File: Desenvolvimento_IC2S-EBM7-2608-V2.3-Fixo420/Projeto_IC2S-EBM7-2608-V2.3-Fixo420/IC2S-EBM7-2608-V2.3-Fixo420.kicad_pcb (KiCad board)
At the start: 4 copper layers, 60 x 60 mm, 146 parts, among them P1 M20-7822046, P2 M20-7821446, T1 TP_+24V, T2 TP_GND_ADC_P1, T3 TP_DGND, T4 TP_+5V_REG, T5 TP_+3.3V_DIG, T6 TP_+3.3V_ANA, T7 TP_GND_ADC, T8 TP_+24V_ADC, U1 R-78HB5.0-0.5L, U10 TPS26613DDFR, U11 TPS26613DDFR, U12 TPS7A4001DGN, U13 LP5907MFX-2.5, U2 SPX3819M5-L-3-3/TR, U3 SPX3819M5-L-3-3/TR, U4 TL431B, U5 ISO7141CCDBQR, U6 AD7124-8BCPZ, U7 ADR4525BRZ, U8 TPS26613DDFR, U9 TPS26613DDFR

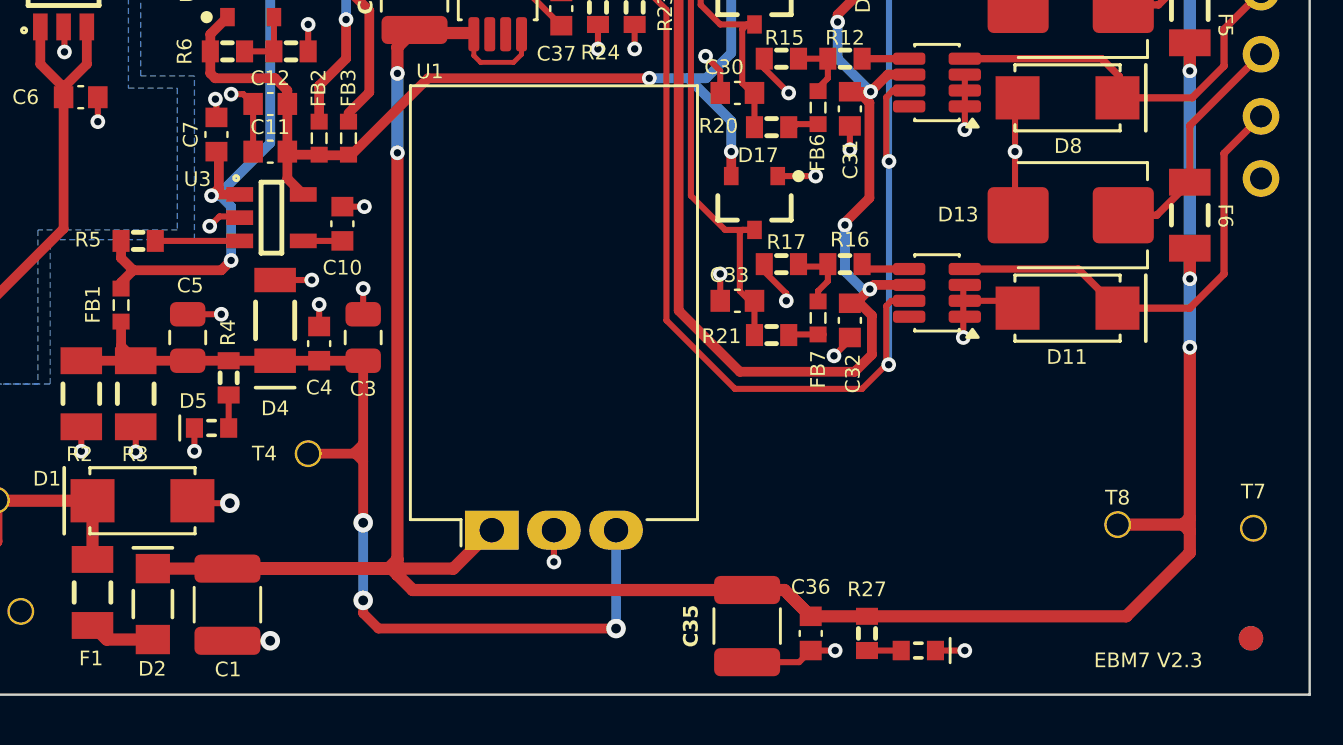
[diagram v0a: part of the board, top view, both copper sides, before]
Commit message: Condensadores do U1 junto dos pinos; pacote de fabricacao regenerado
PCB (28-09 18:19):
- C1 (10 uF/100 V, entrada do R-78HB) a 2,94 mm do pino 1 (era 10,9 mm).
- C3 (22 uF, saida) a 2,32 mm do pino 3 (era 12,4 mm). Recom R-78HB-0.5:
  "C1 and C2 are required and should be fitted close to the converter pins".
- C35/C36/R27 (folha 06) afastados do bordo: C35 de 0,53 para 2,23 mm.
- DRC com paridade: 0 erros, 0 desligados, paridade 0; 1 aviso cosmetico
  (texto C35 sobre o pad do C36).

Doc: corrigida a atribuicao errada do C35 ao U1 e o "C1/C2 do U1" (nomes do
datasheet, nao referencias da placa).

Fabricacao: Gerbers, furacao, PnP, stencil, BOM, vistas, STEP e PDF do
esquematico regenerados desta placa (18:23).

Co-Authored-By: Claude Opus 5.5 (1M context) <noreply@anthropic.com>
Claude-Session: https://claude.ai/code/session_01KPnkiJQKrkjgRqqw9M78ie
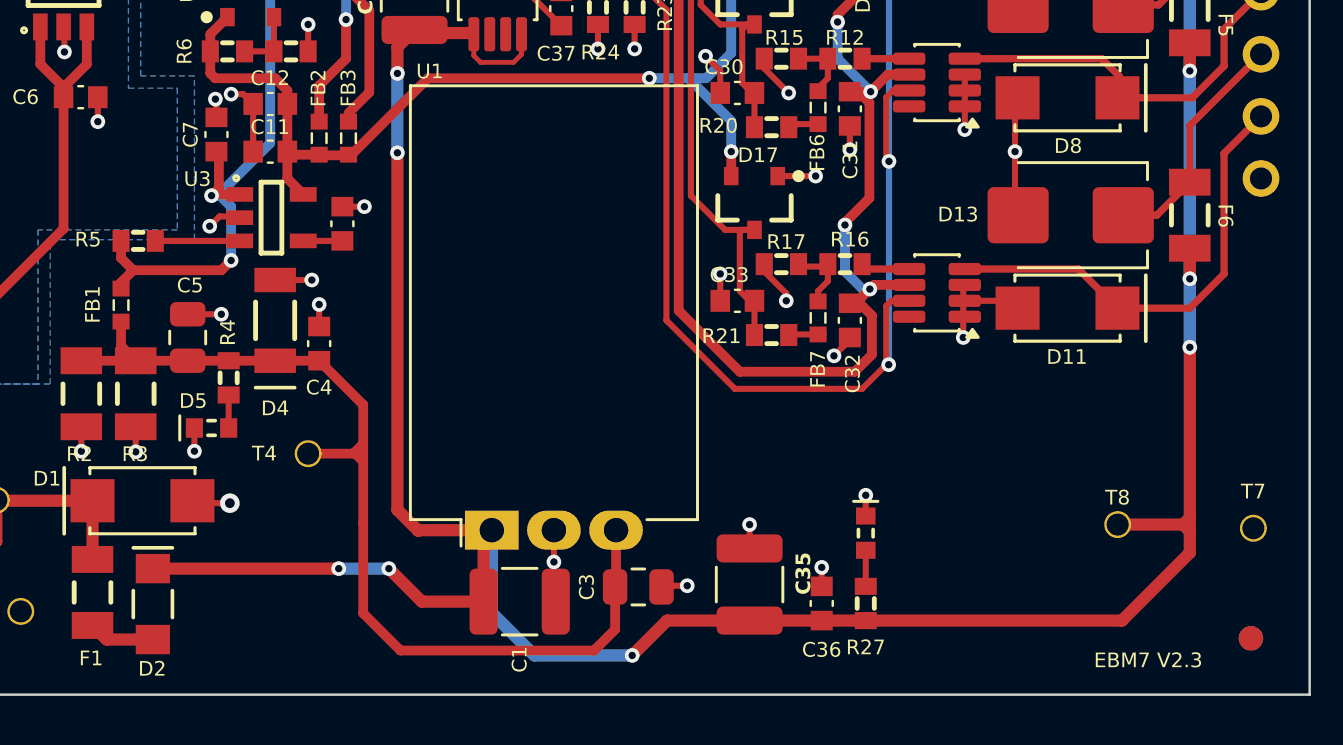
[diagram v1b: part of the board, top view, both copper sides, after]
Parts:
- moved C3 15.2 mm to (151.1, 130.6), turned to 180 degrees
- moved C1 12.0 mm to (146.2, 131.2), turned to 0 degrees
- moved D18 5.26 mm to (160.3, 128.4), turned to -90 degrees
- moved C35 1.70 mm to (155.6, 130.5), turned to 90 degrees
- moved C36 1.31 mm to (158.6, 131.3), turned to 90 degrees
- moved R27 1.23 mm to (160.3, 131.3), turned to 90 degrees
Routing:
- net +24V_ADC: track 129.0 -> 124.3 mm, vias 7 -> 10
- net GND_ADC: track 141.2 -> 137.2 mm
- net +5V_REG: track 42.0 -> 41.7 mm, vias 3 -> 0

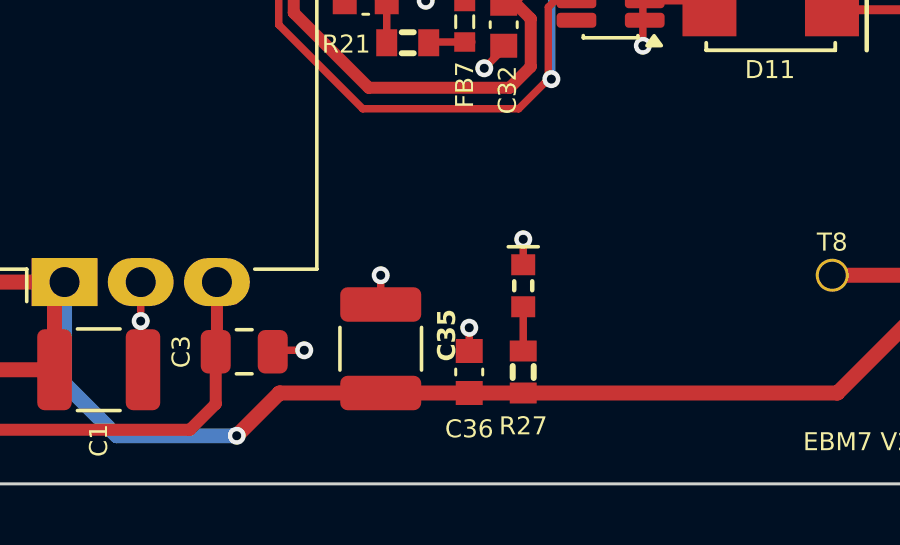
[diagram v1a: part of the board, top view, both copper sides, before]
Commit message: Limpeza do ERC/DRC: fio solto e rotulo duplicado na folha 5, notas do C1 na folha 2, texto do C35
- 05_adc: removido o troco de fio de 1,27 mm em (128,27; 78,74)-(128,27; 80,01)
  com a junction que so existia por ele (extremo sem ligacao no ERC), e o
  rotulo local +2.5_VREF sobreposto ao global em (236,22; 83,82).
- 02_entrada: notas 4 e 12 falavam de "C1/C13" da numeracao antiga; o C13 e
  hoje o bypass do VCC2 do U5. A entrada do U1 (R-78HB) e o C1.
- PCB: texto de serigrafia ${REFERENCE} do C35 afastado do pad do C36.

Netlist do kicad-cli identica pino a pino antes/depois (104 redes;
+2.5_VREF = C24, C25, R8, U6.20, U7.6). DRC com paridade: 0 erros, 0 avisos,
0 desligados, paridade 0. Pacote de fabricacao regenerado.

Co-Authored-By: Claude Opus 5.5 (1M context) <noreply@anthropic.com>
Claude-Session: https://claude.ai/code/session_01KPnkiJQKrkjgRqqw9M78ie
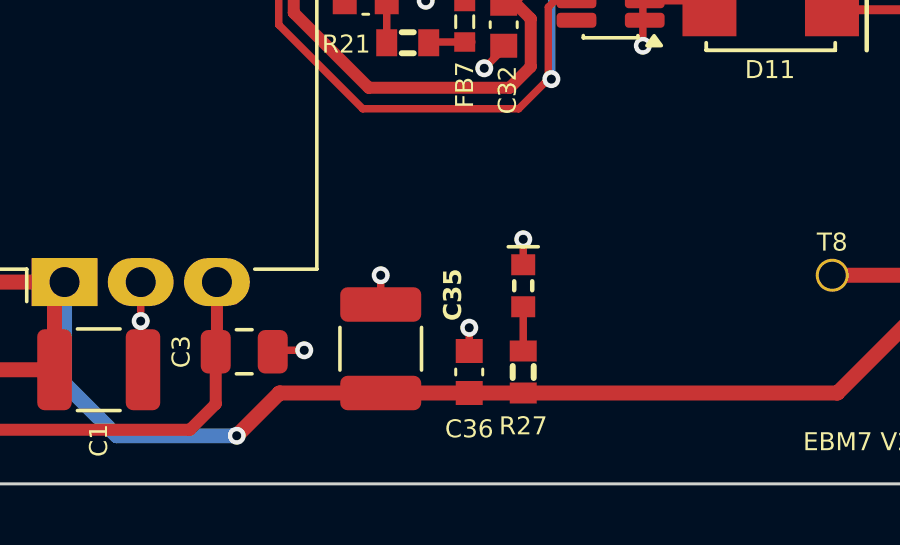
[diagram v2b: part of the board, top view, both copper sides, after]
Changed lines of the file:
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@@
 		)
 		(fp_text user "${REFERENCE}"
-			(at 0.45 2.2 90)
+			(at 1.8 2.4 90)
 			(layer "F.SilkS")
 			(effects

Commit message: PCB: actualizada a partir do esquemático do limitador discreto (sem posicionar)
Equivalente ao F8 (Update PCB from Schematic), feito com ferramentas/atualizar_pcb.py:
- saem U8-U12, R22-R26, C26, C29, C31, C32, C37 e C38 (16);
- entram Q1-Q8, R40-R48, D26 e C50 (19), estacionados abaixo da placa, um canal por linha;
- D6/D7/D8/D11: DO-214 -> DO-214AA (SMBJ36A-13-F), rodados 180 graus. O pad 1 do DO-214AA fica do
  lado oposto ao do DO-214; sem a rotação, a pista AINk caía no pad de GND_ADC;
- R13-R15/R17: 0603R -> 1206R (TNPW1206110RBEEA);
- R10/R11/R12/R16 pad 2 passam a Net-(Q5..Q8-E); as 5 pistas dessas redes seguem o pad;
- U2, C6, C8, C9, T3 e T5 re-ligados ao símbolo pela referência: passaram da folha 3 para a 4 sem
  actualizar a PCB, e o F8 por defeito duplicava-os ou apagava-os. C49 só tinha a folha desactualizada.
Nada mais muda: 882 pistas/vias com a mesma geometria, 11 zonas iguais, sem refill.

DRC: paridade com o esquemático 0 (eram 59). Ficam 104 violações e 44 não ligados, todos do layout
por fazer:
- 8 curtos, 6 clearance e 8 mask bridge: os R13-R17 1206 sobre as pistas AINk_ADC;
- 20 courtyards: 1206 e SMB no sítio antigo;
- 43 pistas soltas do roteamento antigo;
- as peças novas por rotear.
Não fabricar como está.

Co-Authored-By: Claude Opus 5.5 (1M context) <noreply@anthropic.com>
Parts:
- removed C26, C29, C31, C32, C37: 100nF/50V, EBM7_V23:0603C
- removed C38: 10uF/50V, EBM7_V23:C_1206_3216Metric
- removed R22: 11k5, EBM7_V23:0603R
- removed R23, R24: 6k65, EBM7_V23:0603R
- removed R25: 93k1, EBM7_V23:0603R
- removed R26: 10k, EBM7_V23:0603R
- removed U10, U11, U8, U9: TPS26613DDFR, EBM7_V23:SOT-23-8
- removed U12: TPS7A4001DGN, EBM7_V23:HVSSOP-8-1EP
- added C50: 100nF/50V, EBM7_V23:0603C, F.Cu at (124.5, 181.1)
- added D26: BZT52H-C10, EBM7_V23:SOD-123F, F.Cu at (133.5, 181.1)
- added Q1: BSP297, EBM7_V23:SOT-223-3_TabPin2, F.Cu at (124.5, 145.1)
- added Q2: BSP297, EBM7_V23:SOT-223-3_TabPin2, F.Cu at (124.5, 154.1)
- added Q3: BSP297, EBM7_V23:SOT-223-3_TabPin2, F.Cu at (124.5, 163.1)
- added Q4: BSP297, EBM7_V23:SOT-223-3_TabPin2, F.Cu at (124.5, 172.1)
- added Q5: BC847C, EBM7_V23:SOT-23, F.Cu at (133.5, 145.1)
- added Q6: BC847C, EBM7_V23:SOT-23, F.Cu at (133.5, 154.1)
- added Q7: BC847C, EBM7_V23:SOT-23, F.Cu at (133.5, 163.1)
- added Q8: BC847C, EBM7_V23:SOT-23, F.Cu at (133.5, 172.1)
- added R40: 18R, EBM7_V23:0603R, F.Cu at (142.5, 145.1)
- added R41: 18R, EBM7_V23:0603R, F.Cu at (142.5, 154.1)
- added R42: 18R, EBM7_V23:0603R, F.Cu at (142.5, 163.1)
- added R43: 18R, EBM7_V23:0603R, F.Cu at (142.5, 172.1)
- added R44: 100k, EBM7_V23:0603R, F.Cu at (151.5, 145.1)
- added R45: 100k, EBM7_V23:0603R, F.Cu at (151.5, 154.1)
- added R46: 100k, EBM7_V23:0603R, F.Cu at (151.5, 163.1)
- added R47: 100k, EBM7_V23:0603R, F.Cu at (151.5, 172.1)
- added R48: 22k, EBM7_V23:0603R, F.Cu at (142.5, 181.1)
- D11, D6, D7, D8: value 824500301 -> SMBJ36A; footprint EBM7_V23:DO-214 -> EBM7_V23:DO-214AA
- R13, R14, R15, R17: footprint EBM7_V23:0603R -> EBM7_V23:1206R
- turned D11 to 180 degrees
- turned D6 to 180 degrees
- turned D7 to 180 degrees
- turned D8 to 180 degrees
